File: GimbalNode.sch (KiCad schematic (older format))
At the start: 0 parts

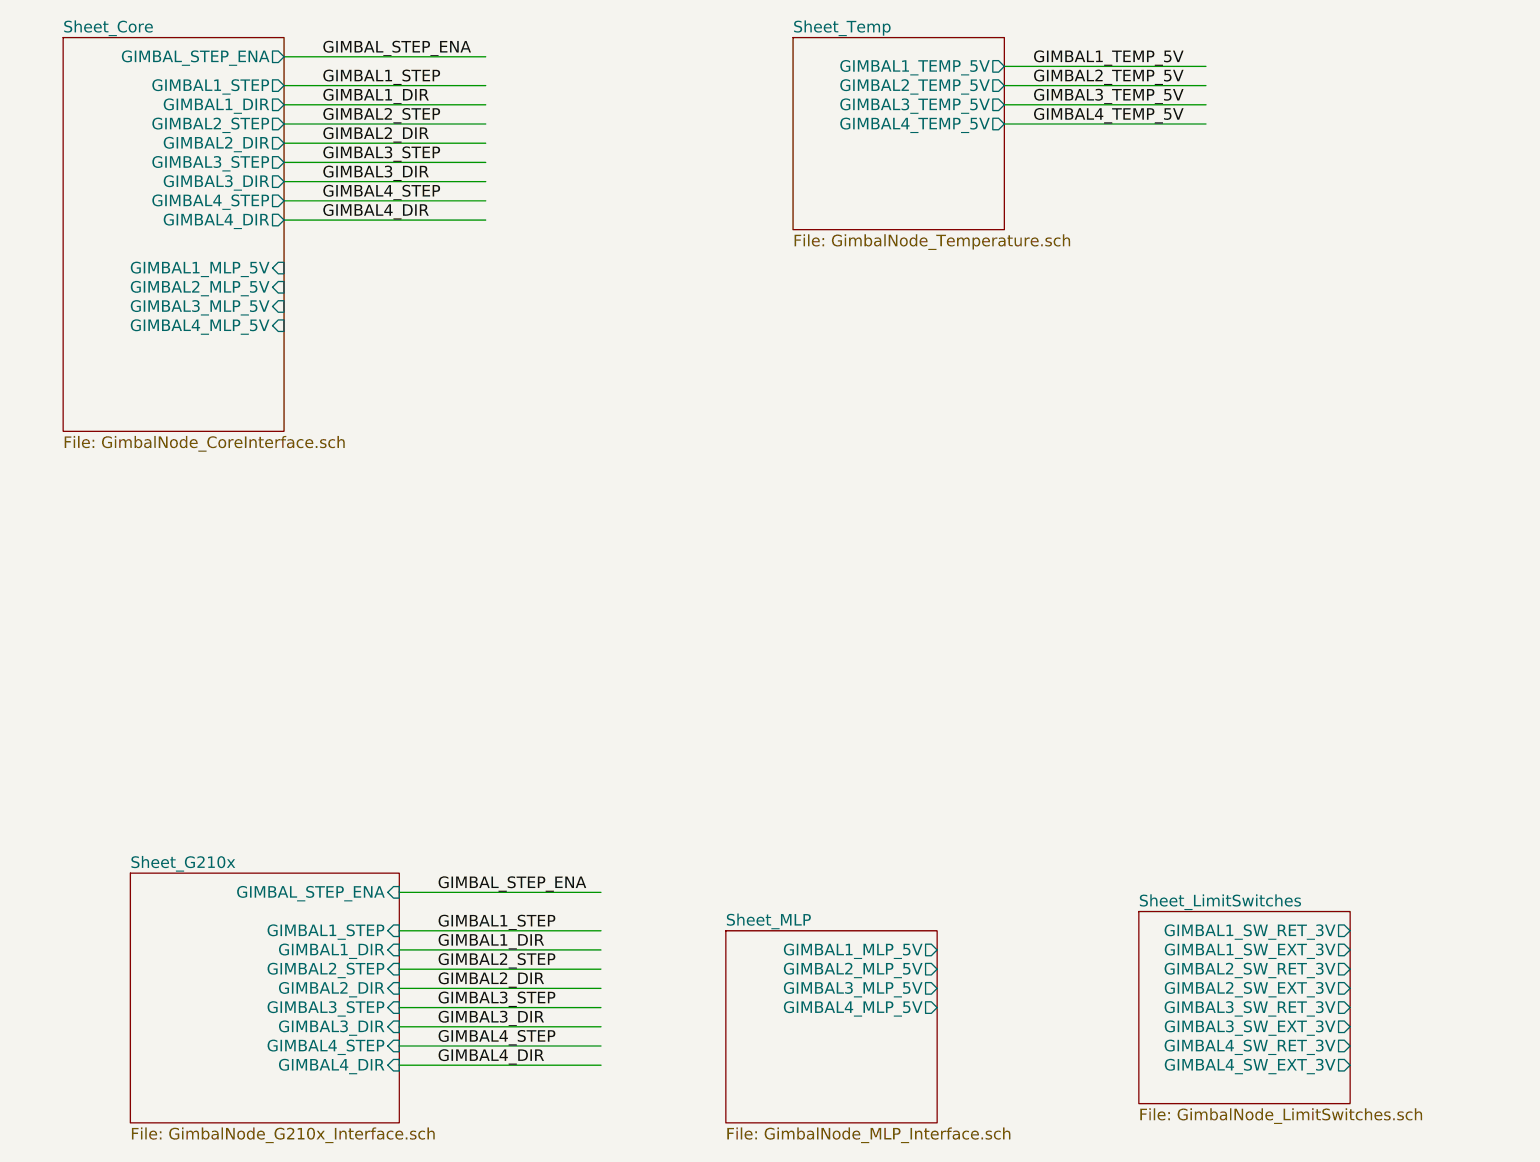
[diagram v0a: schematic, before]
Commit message: Fixup 5V to 3V connections
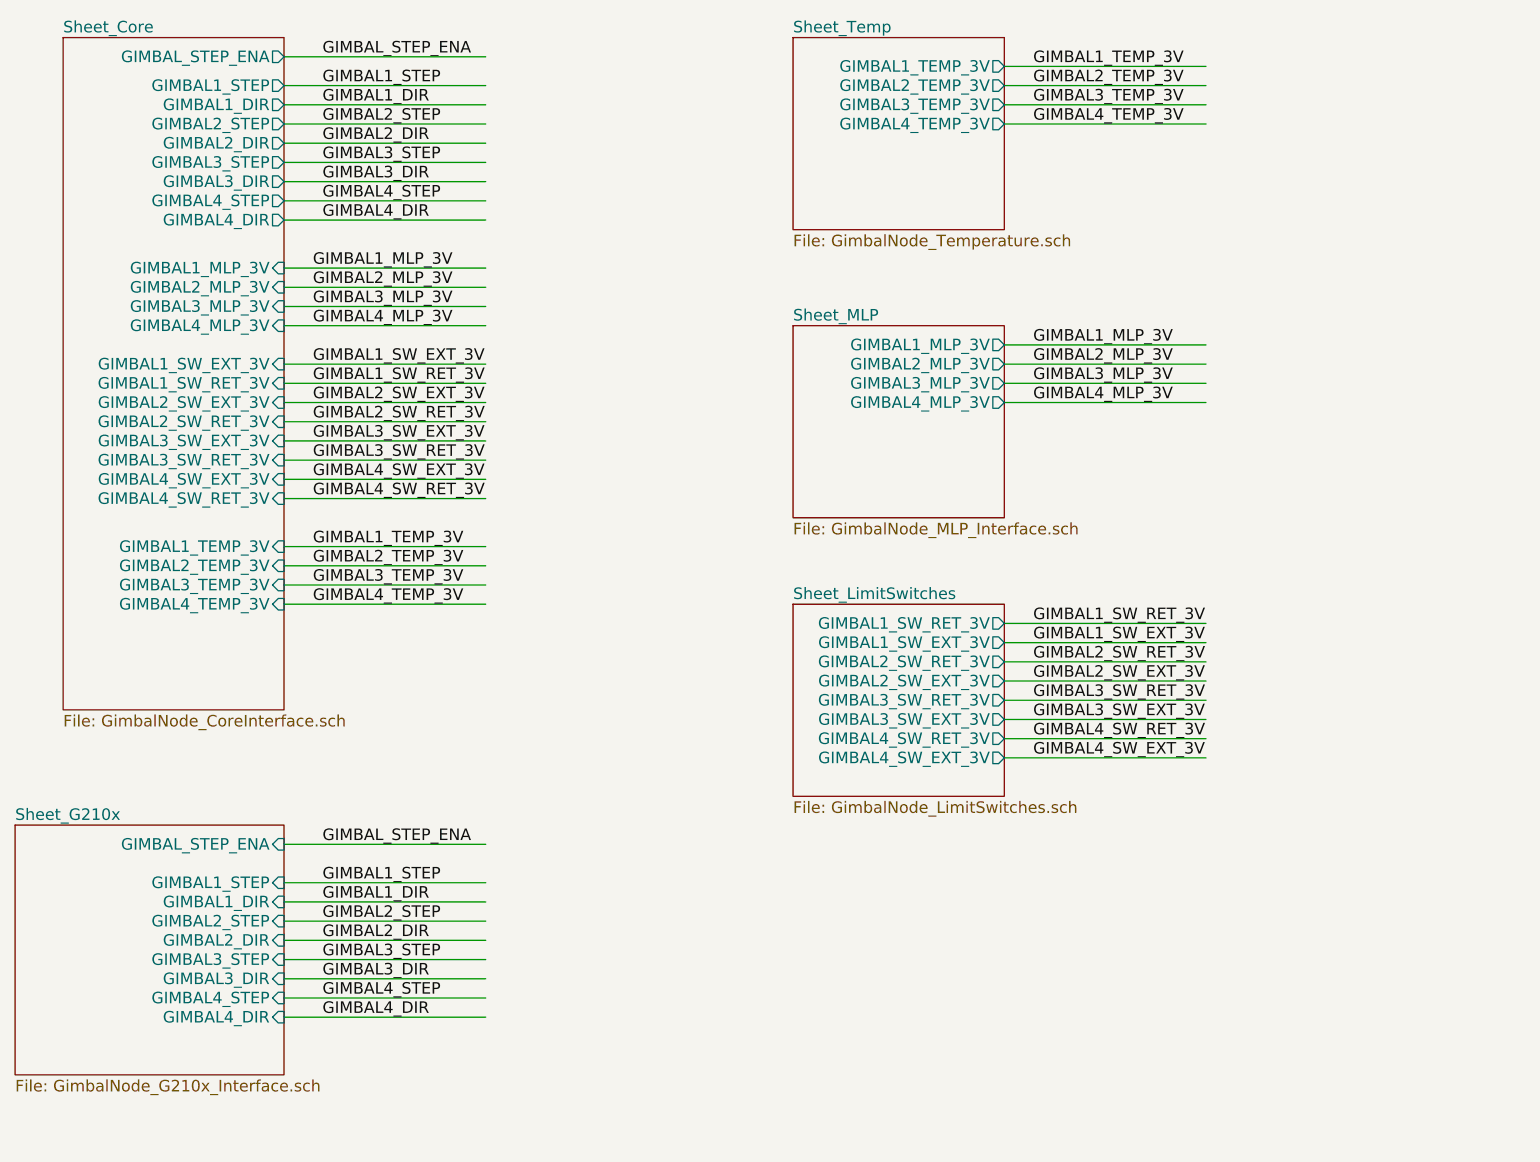
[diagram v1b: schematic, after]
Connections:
- net labels added: GIMBAL1_MLP_3V, GIMBAL1_SW_EXT_3V, GIMBAL1_SW_RET_3V, GIMBAL1_TEMP_3V, GIMBAL2_MLP_3V, GIMBAL2_SW_EXT_3V, GIMBAL2_SW_RET_3V, GIMBAL2_TEMP_3V, GIMBAL3_MLP_3V, GIMBAL3_SW_EXT_3V, GIMBAL3_SW_RET_3V, GIMBAL3_TEMP_3V, GIMBAL4_MLP_3V, GIMBAL4_SW_EXT_3V, GIMBAL4_SW_RET_3V, GIMBAL4_TEMP_3V
- net labels removed: GIMBAL1_TEMP_5V, GIMBAL2_TEMP_5V, GIMBAL3_TEMP_5V, GIMBAL4_TEMP_5V
- wire segments 22 -> 50
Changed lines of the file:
@@
 $EndDescr
 $Sheet
-S 1200 1100 1150 2050
+S 1200 1100 1150 3500
 U 5757E142
 F0 "Sheet_Core" 60
@@
 F9 "GIMBAL4_STEP" O R 2350 1950 60
 F10 "GIMBAL_STEP_ENA" O R 2350 1200 60
-F11 "GIMBAL1_MLP_5V" I R 2350 2300 60
-F12 "GIMBAL2_MLP_5V" I R 2350 2400 60
-F13 "GIMBAL3_MLP_5V" I R 2350 2500 60
-F14 "GIMBAL4_MLP_5V" I R 2350 2600 60
-$EndSheet
-$Sheet
-S 1550 5450 1400 1300
+F11 "GIMBAL1_MLP_3V" I R 2350 2300 60
+F12 "GIMBAL2_MLP_3V" I R 2350 2400 60
+F13 "GIMBAL3_MLP_3V" I R 2350 2500 60
+F14 "GIMBAL4_MLP_3V" I R 2350 2600 60
+F15 "GIMBAL1_SW_RET_3V" I R 2350 2900 60
+F16 "GIMBAL1_SW_EXT_3V" I R 2350 2800 60
+F17 "GIMBAL2_SW_RET_3V" I R 2350 3100 60
+F18 "GIMBAL2_SW_EXT_3V" I R 2350 3000 60
+F19 "GIMBAL3_SW_RET_3V" I R 2350 3300 60
+F20 "GIMBAL3_SW_EXT_3V" I R 2350 3200 60
+F21 "GIMBAL4_SW_RET_3V" I R 2350 3500 60
+F22 "GIMBAL4_SW_EXT_3V" I R 2350 3400 60
+F23 "GIMBAL3_TEMP_3V" I R 2350 3950 60
+F24 "GIMBAL2_TEMP_3V" I R 2350 3850 60
+F25 "GIMBAL1_TEMP_3V" I R 2350 3750 60
+F26 "GIMBAL4_TEMP_3V" I R 2350 4050 60
+$EndSheet
+$Sheet
+S 950  5200 1400 1300
 U 5757E168
 F0 "Sheet_G210x" 60
 F1 "GimbalNode_G210x_Interface.sch" 60
-F2 "GIMBAL_STEP_ENA" I R 2950 5550 60
-F3 "GIMBAL1_DIR" I R 2950 5850 60
-F4 "GIMBAL1_STEP" I R 2950 5750 60
-F5 "GIMBAL2_STEP" I R 2950 5950 60
-F6 "GIMBAL2_DIR" I R 2950 6050 60
-F7 "GIMBAL3_DIR" I R 2950 6250 60
-F8 "GIMBAL3_STEP" I R 2950 6150 60
-F9 "GIMBAL4_STEP" I R 2950 6350 60
-F10 "GIMBAL4_DIR" I R 2950 6450 60
-$EndSheet
-$Sheet
-S 4650 5750 1100 1000
+F2 "GIMBAL_STEP_ENA" I R 2350 5300 60
+F3 "GIMBAL1_DIR" I R 2350 5600 60
+F4 "GIMBAL1_STEP" I R 2350 5500 60
+F5 "GIMBAL2_STEP" I R 2350 5700 60
+F6 "GIMBAL2_DIR" I R 2350 5800 60
+F7 "GIMBAL3_DIR" I R 2350 6000 60
+F8 "GIMBAL3_STEP" I R 2350 5900 60
+F9 "GIMBAL4_STEP" I R 2350 6100 60
+F10 "GIMBAL4_DIR" I R 2350 6200 60
+$EndSheet
+$Sheet
+S 5000 2600 1100 1000
 U 5757E189
 F0 "Sheet_MLP" 60
 F1 "GimbalNode_MLP_Interface.sch" 60
-F2 "GIMBAL1_MLP_5V" O R 5750 5850 60
-F3 "GIMBAL2_MLP_5V" O R 5750 5950 60
-F4 "GIMBAL3_MLP_5V" O R 5750 6050 60
-F5 "GIMBAL4_MLP_5V" O R 5750 6150 60
-$EndSheet
-$Sheet
-S 6800 5650 1100 1000
+F2 "GIMBAL1_MLP_3V" O R 6100 2700 60
+F3 "GIMBAL2_MLP_3V" O R 6100 2800 60
+F4 "GIMBAL3_MLP_3V" O R 6100 2900 60
+F5 "GIMBAL4_MLP_3V" O R 6100 3000 60
+$EndSheet
+$Sheet
+S 5000 4050 1100 1000
 U 5757E1A2
 F0 "Sheet_LimitSwitches" 60
 F1 "GimbalNode_LimitSwitches.sch" 60
-F2 "GIMBAL1_SW_RET_3V" O R 7900 5750 60
-F3 "GIMBAL1_SW_EXT_3V" O R 7900 5850 60
-F4 "GIMBAL2_SW_RET_3V" O R 7900 5950 60
-F5 "GIMBAL2_SW_EXT_3V" O R 7900 6050 60
-F6 "GIMBAL3_SW_RET_3V" O R 7900 6150 60
-F7 "GIMBAL3_SW_EXT_3V" O R 7900 6250 60
-F8 "GIMBAL4_SW_RET_3V" O R 7900 6350 60
-F9 "GIMBAL4_SW_EXT_3V" O R 7900 6450 60
+F2 "GIMBAL1_SW_RET_3V" O R 6100 4150 60
+F3 "GIMBAL1_SW_EXT_3V" O R 6100 4250 60
+F4 "GIMBAL2_SW_RET_3V" O R 6100 4350 60
+F5 "GIMBAL2_SW_EXT_3V" O R 6100 4450 60
+F6 "GIMBAL3_SW_RET_3V" O R 6100 4550 60
+F7 "GIMBAL3_SW_EXT_3V" O R 6100 4650 60
+F8 "GIMBAL4_SW_RET_3V" O R 6100 4750 60
+F9 "GIMBAL4_SW_EXT_3V" O R 6100 4850 60
 $EndSheet
 $Sheet
@@
 F0 "Sheet_Temp" 60
 F1 "GimbalNode_Temperature.sch" 60
-F2 "GIMBAL1_TEMP_5V" O R 6100 1250 60
-F3 "GIMBAL2_TEMP_5V" O R 6100 1350 60
-F4 "GIMBAL3_TEMP_5V" O R 6100 1450 60
-F5 "GIMBAL4_TEMP_5V" O R 6100 1550 60
-$EndSheet
-Wire Wire Line
-	2950 5550 4000 5550
-Wire Wire Line
-	2950 5750 4000 5750
-Text Label 3150 5550 0    60   ~ 0
+F2 "GIMBAL1_TEMP_3V" O R 6100 1250 60
+F3 "GIMBAL2_TEMP_3V" O R 6100 1350 60
+F4 "GIMBAL3_TEMP_3V" O R 6100 1450 60
+F5 "GIMBAL4_TEMP_3V" O R 6100 1550 60
+$EndSheet
+Wire Wire Line
+	2350 5300 3400 5300
+Wire Wire Line
+	2350 5500 3400 5500
+Text Label 2550 5300 0    60   ~ 0
 GIMBAL_STEP_ENA
-Text Label 3150 5750 0    60   ~ 0
+Text Label 2550 5500 0    60   ~ 0
 GIMBAL1_STEP
 Wire Wire Line
-	2950 5850 4000 5850
-Text Label 3150 5850 0    60   ~ 0
+	2350 5600 3400 5600
+Text Label 2550 5600 0    60   ~ 0
 GIMBAL1_DIR
 Wire Wire Line
-	2950 5950 4000 5950
-Text Label 3150 5950 0    60   ~ 0
+	2350 5700 3400 5700
+Text Label 2550 5700 0    60   ~ 0
 GIMBAL2_STEP
 Wire Wire Line
-	2950 6050 4000 6050
-Text Label 3150 6050 0    60   ~ 0
+	2350 5800 3400 5800
+Text Label 2550 5800 0    60   ~ 0
 GIMBAL2_DIR
 Wire Wire Line
-	2950 6150 4000 6150
-Text Label 3150 6150 0    60   ~ 0
+	2350 5900 3400 5900
+Text Label 2550 5900 0    60   ~ 0
 GIMBAL3_STEP
 Wire Wire Line
-	2950 6250 4000 6250
-Text Label 3150 6250 0    60   ~ 0
+	2350 6000 3400 6000
+Text Label 2550 6000 0    60   ~ 0
 GIMBAL3_DIR
 Wire Wire Line
-	2950 6350 4000 6350
-Text Label 3150 6350 0    60   ~ 0
+	2350 6100 3400 6100
+Text Label 2550 6100 0    60   ~ 0
 GIMBAL4_STEP
 Wire Wire Line
-	2950 6450 4000 6450
-Text Label 3150 6450 0    60   ~ 0
+	2350 6200 3400 6200
+Text Label 2550 6200 0    60   ~ 0
 GIMBAL4_DIR
 Wire Wire Line
@@
 	6100 1250 7150 1250
 Text Label 6250 1250 0    60   ~ 0
-GIMBAL1_TEMP_5V
+GIMBAL1_TEMP_3V
 Wire Wire Line
 	6100 1350 7150 1350
 Text Label 6250 1350 0    60   ~ 0
-GIMBAL2_TEMP_5V
+GIMBAL2_TEMP_3V
 Wire Wire Line
 	6100 1450 7150 1450
 Text Label 6250 1450 0    60   ~ 0
-GIMBAL3_TEMP_5V
+GIMBAL3_TEMP_3V
 Wire Wire Line
 	6100 1550 7150 1550
 Text Label 6250 1550 0    60   ~ 0
-GIMBAL4_TEMP_5V
+GIMBAL4_TEMP_3V
+Wire Wire Line
+	2350 3750 3400 3750
+Text Label 2500 3750 0    60   ~ 0
+GIMBAL1_TEMP_3V
+Wire Wire Line
+	2350 3850 3400 3850
+Text Label 2500 3850 0    60   ~ 0
+GIMBAL2_TEMP_3V
+Wire Wire Line
+	2350 3950 3400 3950
+Text Label 2500 3950 0    60   ~ 0
+GIMBAL3_TEMP_3V
+Wire Wire Line
+	2350 4050 3400 4050
+Text Label 2500 4050 0    60   ~ 0
+GIMBAL4_TEMP_3V
+Wire Wire Line
+	6100 2700 7150 2700
+Text Label 6250 2700 0    60   ~ 0
+GIMBAL1_MLP_3V
+Wire Wire Line
+	6100 2800 7150 2800
+Text Label 6250 2800 0    60   ~ 0
+GIMBAL2_MLP_3V
+Wire Wire Line
+	6100 2900 7150 2900
+Text Label 6250 2900 0    60   ~ 0
+GIMBAL3_MLP_3V
+Wire Wire Line
+	6100 3000 7150 3000
+Text Label 6250 3000 0    60   ~ 0
+GIMBAL4_MLP_3V
+Wire Wire Line
+	2350 2300 3400 2300
+Text Label 2500 2300 0    60   ~ 0
+GIMBAL1_MLP_3V
+Wire Wire Line
+	2350 2400 3400 2400
+Text Label 2500 2400 0    60   ~ 0
+GIMBAL2_MLP_3V
+Wire Wire Line
+	2350 2500 3400 2500
+Text Label 2500 2500 0    60   ~ 0
+GIMBAL3_MLP_3V
+Wire Wire Line
+	2350 2600 3400 2600
+Text Label 2500 2600 0    60   ~ 0
+GIMBAL4_MLP_3V
+Wire Wire Line
+	6100 4150 7150 4150
+Text Label 6250 4150 0    60   ~ 0
+GIMBAL1_SW_RET_3V
+Wire Wire Line
+	6100 4250 7150 4250
+Text Label 6250 4250 0    60   ~ 0
+GIMBAL1_SW_EXT_3V
+Wire Wire Line
+	6100 4350 7150 4350
+Text Label 6250 4350 0    60   ~ 0
+GIMBAL2_SW_RET_3V
+Wire Wire Line
+	6100 4450 7150 4450
+Text Label 6250 4450 0    60   ~ 0
+GIMBAL2_SW_EXT_3V
+Wire Wire Line
+	6100 4550 7150 4550
+Text Label 6250 4550 0    60   ~ 0
+GIMBAL3_SW_RET_3V
+Wire Wire Line
+	6100 4650 7150 4650
+Text Label 6250 4650 0    60   ~ 0
+GIMBAL3_SW_EXT_3V
+Wire Wire Line
+	6100 4750 7150 4750
+Text Label 6250 4750 0    60   ~ 0
+GIMBAL4_SW_RET_3V
+Wire Wire Line
+	6100 4850 7150 4850
+Text Label 6250 4850 0    60   ~ 0
+GIMBAL4_SW_EXT_3V
+Wire Wire Line
+	2350 2800 3400 2800
+Text Label 2500 2900 0    60   ~ 0
+GIMBAL1_SW_RET_3V
+Wire Wire Line
+	2350 2900 3400 2900
+Text Label 2500 2800 0    60   ~ 0
+GIMBAL1_SW_EXT_3V
+Wire Wire Line
+	2350 3000 3400 3000
+Text Label 2500 3100 0    60   ~ 0
+GIMBAL2_SW_RET_3V
+Wire Wire Line
+	2350 3100 3400 3100
+Text Label 2500 3000 0    60   ~ 0
+GIMBAL2_SW_EXT_3V
+Wire Wire Line
+	2350 3200 3400 3200
+Text Label 2500 3300 0    60   ~ 0
+GIMBAL3_SW_RET_3V
+Wire Wire Line
+	2350 3300 3400 3300
+Text Label 2500 3200 0    60   ~ 0
+GIMBAL3_SW_EXT_3V
+Wire Wire Line
+	2350 3400 3400 3400
+Text Label 2500 3500 0    60   ~ 0
+GIMBAL4_SW_RET_3V
+Wire Wire Line
+	2350 3500 3400 3500
+Text Label 2500 3400 0    60   ~ 0
+GIMBAL4_SW_EXT_3V
 $EndSCHEMATC

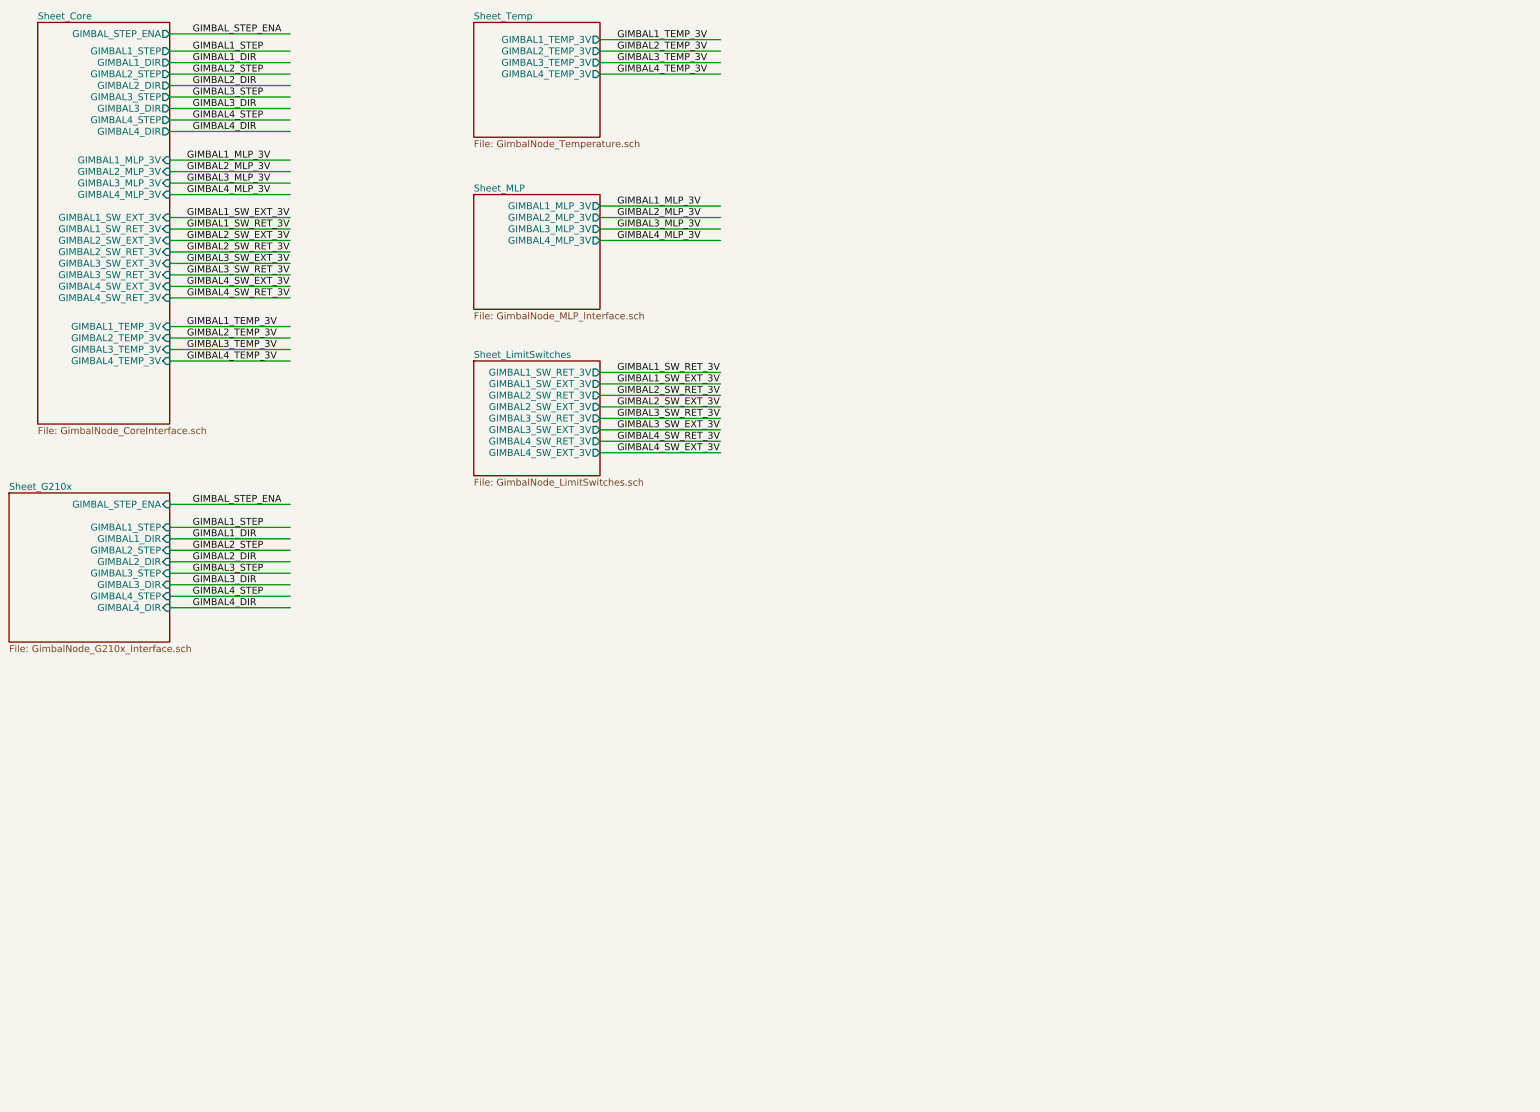
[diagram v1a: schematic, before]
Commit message: Update connectors, diodes, add zener's and anotate.
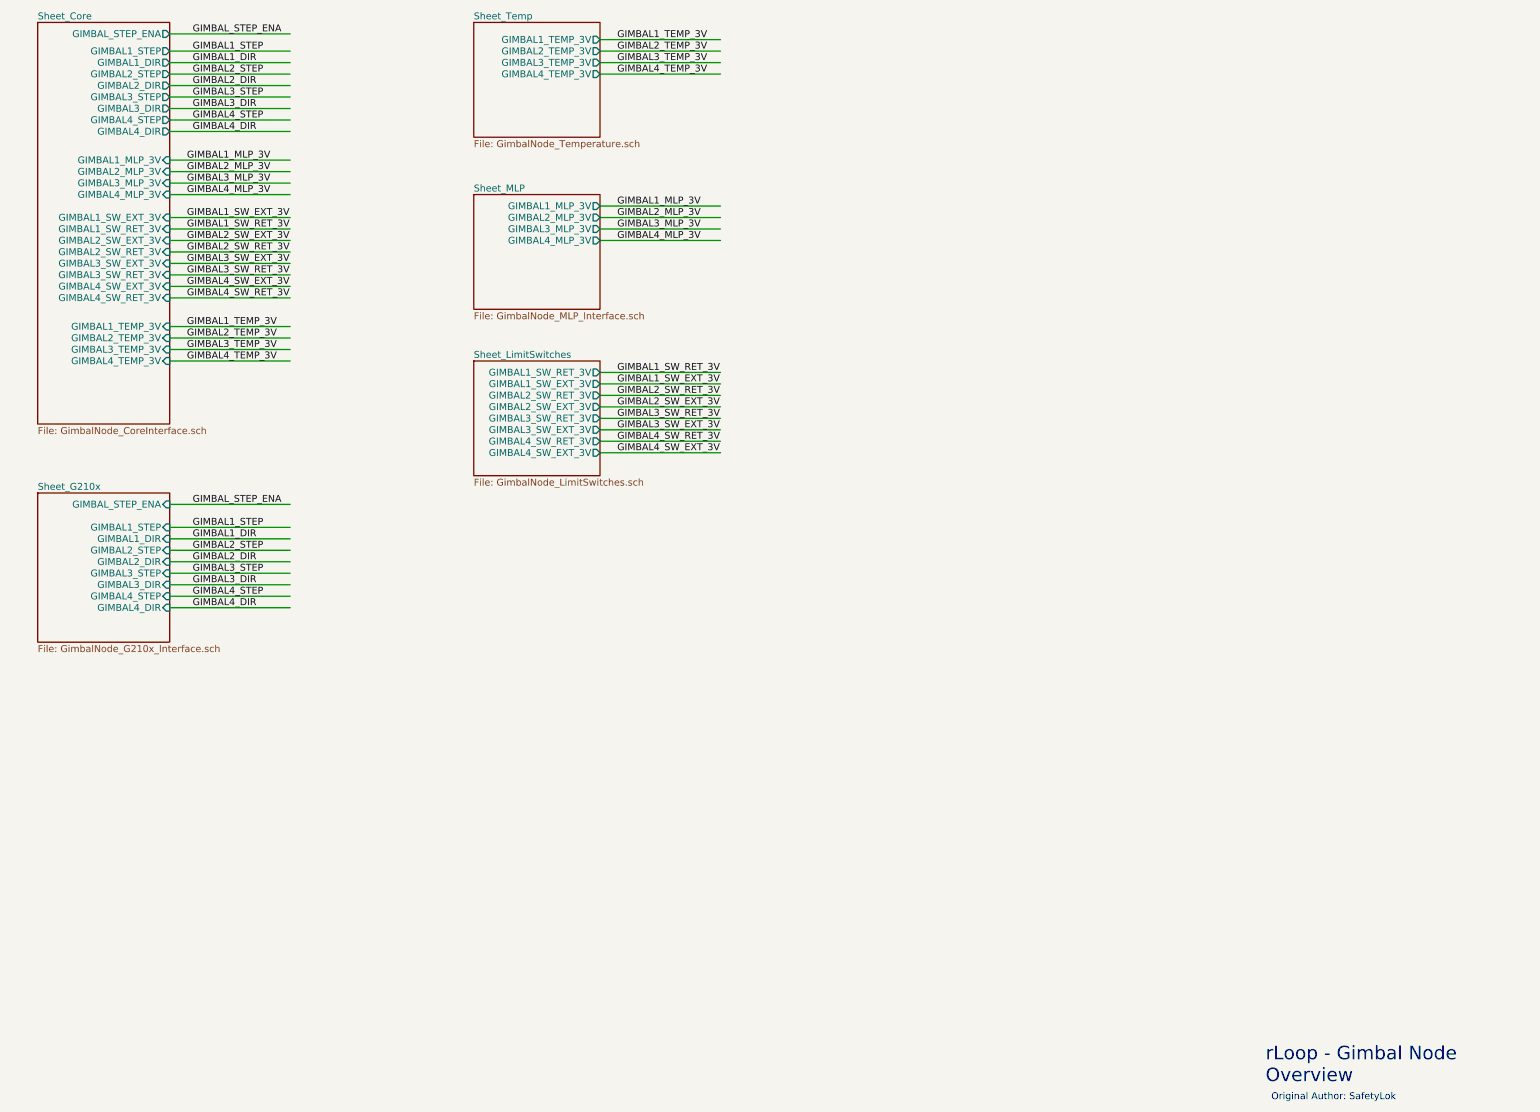
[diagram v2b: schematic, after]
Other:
- note added: "Original Author: SafetyLok"
- note added: "rLoop - Gimbal Node\nOverview\n"
